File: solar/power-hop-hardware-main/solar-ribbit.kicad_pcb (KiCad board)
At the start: 6 copper layers, 84 x 50 mm, 171 parts, among them CN1 USB4105-GF-A, J1 KEYSTONE_254, J10 BM04B-SRSS-TB, J11 CONMHF1-SMD-G-T, J12 FTSH-105-01-L-DV-K, J13 SF72S006VBDR2500, J14 10129380-902001BLF, J15 FTSH-105-01-L-DV-K, J16 S2B-PH-SM4-TB, J2 KEYSTONE_254, J3 3.5mm/1.1mm, J4 10129380-902001BLF, J5 10129380-902001BLF, J6 10129380-902001BLF, J7 10129380-902001BLF, J8 10129380-902001BLF, J9 10129380-902001BLF, Q1 DMN1019UFDE-7, Q2 DMN1019UFDE-7, Q3 DMN1019UFDE-7, Q4 DMN1019UFDE-7, Q5 SSM3J355R,LF, Q6 EFC3J018NUZTDG, SW1 PTS636SM50JSMTR LFS, SW2 PTS636SM50JSMTR LFS, U1 nRF9151-LACA, U10 NRF52833-QDAA-B-R7, U11 BQ298000, U2 SKY65943-11, U3 EMIF03-SIM02M8, U4 MX25V8035FZUI, U5 BQ25798, U6 TPS631010YBGR, U7 TPS22995RZFR, U8 EXC-34CE121U, U9 USBLC6-4SC6

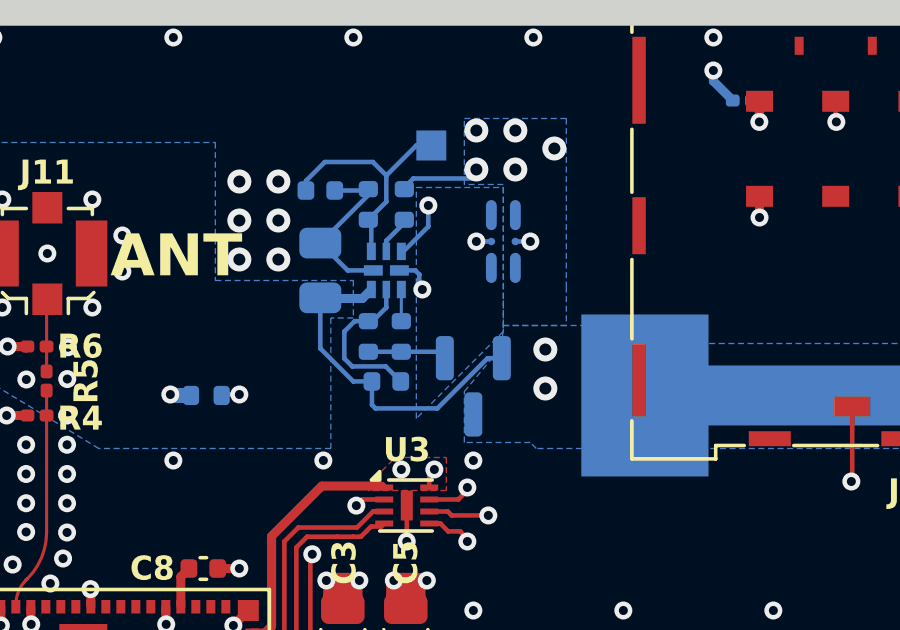
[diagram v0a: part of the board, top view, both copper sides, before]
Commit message: Remapped Q5 and rerouted traces
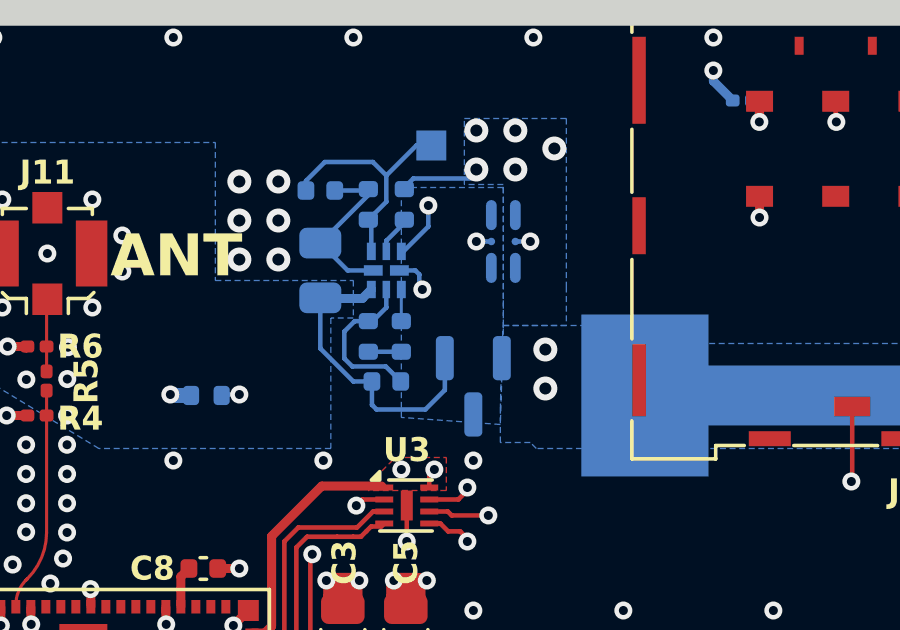
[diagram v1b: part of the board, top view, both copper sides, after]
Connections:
- Q5 pad 1: /Battery Protection/BAT_P_POL -> /BAT_N
- Q5 pad 2: /BAT_N -> /BAT_P
- Q5 pad 3: /BAT_P -> /Battery Protection/BAT_P_POL
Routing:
- net /Battery Protection/BAT_P_POL: track 2.64 -> 1.10 mm
- net /BAT_N: track 27.8 -> 26.8 mm
